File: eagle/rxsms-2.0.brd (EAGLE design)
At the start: 159 x 120.5 mm, 164 parts, among them Q1 opt, Q10 BSS123, Q11 BSS123, Q12 BSS123, Q2 BSS123, Q3 BSS123, Q4 BSS123, Q5 BSS123, Q6 BSS123, Q7 BSS123, Q8 BSS123, Q9 BSS123, T10_SODS SWITCH_LED, T1_LO SMS_IP67, T2_SOE SMS_IP67, T3_SOE SWITCH_LED, T4_PWR SMS_IP67, T5_ERRINH SMS_IP67, T6_PWR SWITCH_LED, T7_ERRINH SWITCH_LED, T8_LO SWITCH_LED, T9_SODS SMS_IP67, U1 MAX3232ESE, U2 XMEGA-A4UTQFP, U3 TSR_1-2450, U4 LM1117, U5 NC7WZ17P6X, U6 ADUM3160, U7 TPS73125, U8 NUP2202W1, X1 PN61729-S, X5 RLP2-200-500

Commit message: continued layout
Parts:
- moved C9 1.27 mm to (74.3, 21.6)
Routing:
- net RESERVED_IO_1: track 21.2 -> 18.3 mm
- net RESERVED_IO_0: track 25.2 -> 22.3 mm
- net GND: track 968.7 -> 966.0 mm, vias 17 -> 19
- net USB_VBUS: track 63.5 -> 62.8 mm
- net RESERVED_UART1_RX: track 14.1 -> 14.8 mm
- net N$16: track 41.2 -> 40.4 mm
- net +3V3: track 505.8 -> 506.5 mm

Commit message: fix: use correct lib name for TEN 3-2410N DCDC iso regulator
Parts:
- U$10: value TES3-4810WI -> TEN3-2410N; device TES3-4810WI:TES3-4810WI -> TEN3:TEN3-2410N
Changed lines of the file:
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@@
 <attribute name="OC_FARNELL" value="unknown" x="87.63" y="111.76" size="1.778" layer="27" display="off"/>
 </element>
-<element name="U$10" library="TES3-4810WI" package="TES3-4810WI" value="TES3-4810WI" x="58.42" y="48.26" rot="R180">
+<element name="U$10" library="TEN3" package="TEN3-2410N" value="TEN3-2410N" x="58.42" y="48.26" rot="R180">
 <attribute name="OC_RS" value="801-9330" x="58.42" y="48.26" size="1.778" layer="27" rot="R180" display="off"/>
 </element>

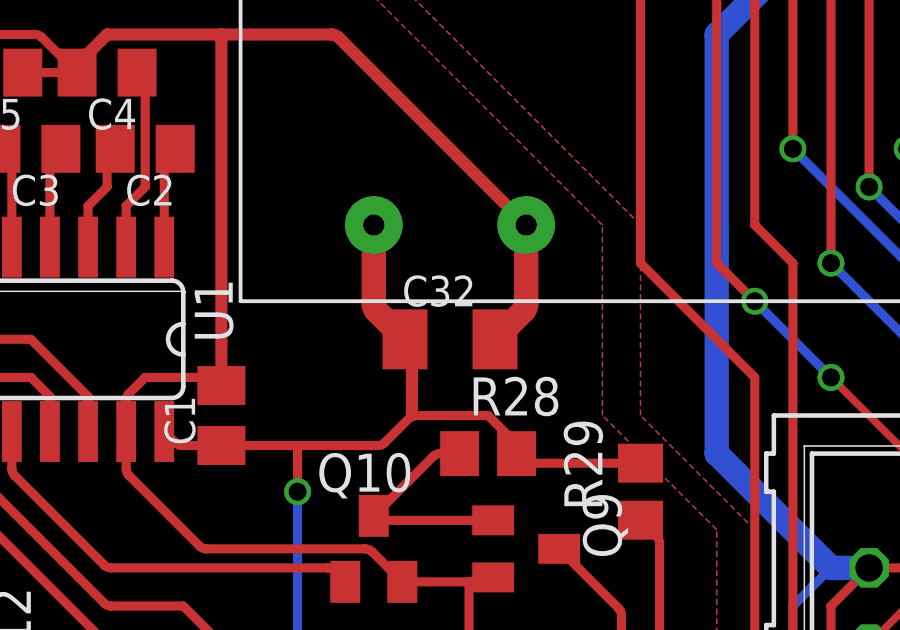
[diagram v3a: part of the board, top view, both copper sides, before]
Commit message: more OC added
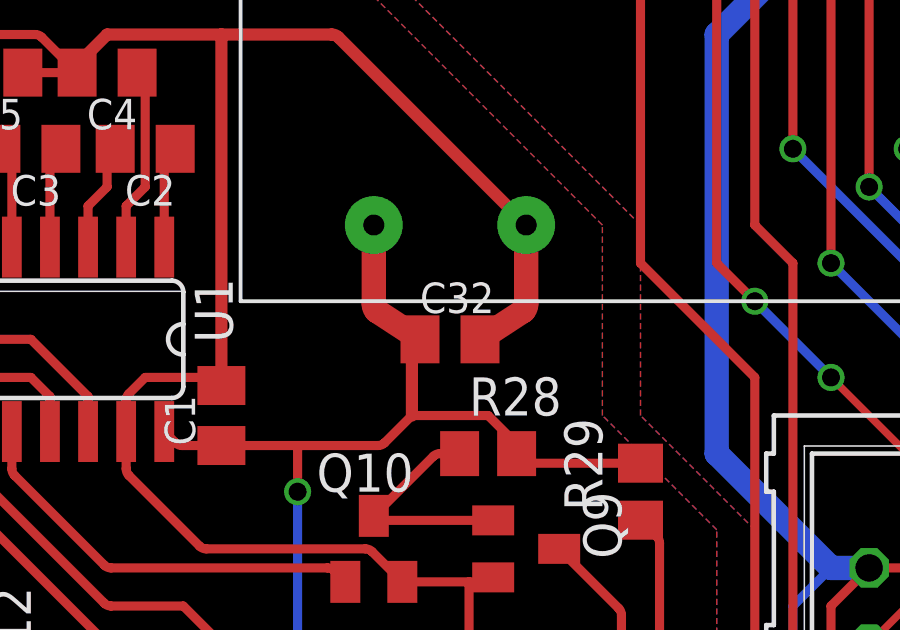
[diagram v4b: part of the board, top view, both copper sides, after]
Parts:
- C32: device rcl:C1206K -> rcl:C0805K
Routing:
- net VDD: track 65.6 -> 66.2 mm
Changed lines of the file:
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@@
 <attribute name="OC_FARNELL" value="1667008" x="83.82" y="29.21" size="1.778" layer="27" rot="R270" display="off"/>
 </element>
-<element name="U3" library="_traco_tsr-1" package="TSR-1" value="TSR_1-2450" x="78.74" y="91.44" rot="R270"/>
+<element name="U3" library="_traco_tsr-1" package="TSR-1" value="TSR_1-2450" x="78.74" y="91.44" rot="R270">
+<attribute name="OC_FARNELL" value="1696320" x="78.74" y="91.44" size="1.778" layer="27" rot="R270" display="off"/>
+</element>
 <element name="C12" library="rcl" package="C0805K" value="4u7/50V" x="62.23" y="85.09"/>
 <element name="C13" library="rcl" package="C0805K" value="4u7/50V" x="80.01" y="83.82"/>
@@
 <attribute name="OC_FARNELL" value="1887308" x="18.415" y="85.09" size="1.778" layer="27" rot="R270" display="off"/>
 </element>
-<element name="R4" library="rcl" package="R0805" value="22k" x="31.75" y="72.39" rot="R180"/>
-<element name="U$6" library="BTS6134" package="TO-252-5-1" value="BTS6143" x="26.67" y="104.14" rot="R270"/>
+<element name="R4" library="rcl" package="R0805" value="22k" x="31.75" y="72.39" rot="R180">
+<attribute name="OC_FARNELL" value="2303686" x="31.75" y="72.39" size="1.778" layer="27" rot="R180" display="off"/>
+</element>
+<element name="U$6" library="BTS6134" package="TO-252-5-1" value="BTS6143" x="26.67" y="104.14" rot="R270">
+<attribute name="OC_FARNELL" value="1440813" x="26.67" y="104.14" size="1.778" layer="27" rot="R270" display="off"/>
+</element>
 <element name="R5" library="rcl" package="R0805" value="10k" x="54.61" y="87.63" rot="R180">
 <attribute name="OC_FARNELL" value="1887308" x="54.61" y="87.63" size="1.778" layer="27" rot="R180" display="off"/>
@@
 <attribute name="OC_FARNELL" value="1887308" x="43.18" y="93.98" size="1.778" layer="27" rot="R270" display="off"/>
 </element>
-<element name="U6" library="adum3160" package="SO-16W" value="ADUM3160" x="113.03" y="10.16" rot="R90"/>
+<element name="U6" library="adum3160" package="SO-16W" value="ADUM3160" x="113.03" y="10.16" rot="R90">
+<attribute name="OC_FARNELL" value="1843660" x="113.03" y="10.16" size="1.778" layer="27" rot="R90" display="off"/>
+</element>
 <element name="C17" library="rcl" package="C0805K" value="&gt;100n/low ESR" x="123.19" y="8.255"/>
-<element name="R12" library="rcl" package="R0805" value="24/1%" x="124.46" y="11.43"/>
+<element name="R12" library="rcl" package="R0805" value="24/1%" x="124.46" y="11.43">
+<attribute name="OC_FARNELL" value="1894163" x="124.46" y="11.43" size="1.778" layer="27" display="off"/>
+</element>
 <element name="C18" library="rcl" package="C0805K" value="&gt;100n/low ESR" x="123.19" y="5.08"/>
-<element name="R13" library="rcl" package="R0805" value="24/1%" x="124.46" y="13.97"/>
+<element name="R13" library="rcl" package="R0805" value="24/1%" x="124.46" y="13.97">
+<attribute name="OC_FARNELL" value="1894163" x="124.46" y="13.97" size="1.778" layer="27" display="off"/>
+</element>
 <element name="C19" library="rcl" package="C0805K" value="&gt;100n/low ESR" x="104.14" y="7.62" rot="R270"/>
 <element name="C20" library="rcl" package="C0805K" value="&gt;100n/low ESR" x="101.6" y="7.62" rot="R270"/>
-<element name="R14" library="rcl" package="R0805" value="24/1%" x="99.6696" y="15.4813"/>
-<element name="R15" library="rcl" package="R0805" value="24/1%" x="97.4344" y="12.0015"/>
+<element name="R14" library="rcl" package="R0805" value="24/1%" x="99.6696" y="15.4813">
+<attribute name="OC_FARNELL" value="1894163" x="99.6696" y="15.4813" size="1.778" layer="27" display="off"/>
+</element>
+<element name="R15" library="rcl" package="R0805" value="24/1%" x="97.4344" y="12.0015">
+<attribute name="OC_FARNELL" value="1894163" x="97.4344" y="12.0015" size="1.778" layer="27" display="off"/>
+</element>
 <element name="U4" library="LM1117" package="TO252" value="LM1117" x="73.66" y="74.93" rot="R90"/>
 <element name="X1" library="con-berg" package="PN61729-S" value="PN61729-S" x="151.206384375" y="11" rot="R90">
@@
 <attribute name="MPN" value="" x="151.206384375" y="11" size="1.778" layer="27" rot="R90" display="off"/>
 <attribute name="MF" value="" x="151.206384375" y="11" size="1.778" layer="27" rot="R90" display="off"/>
-<attribute name="OC_FARNELL" value="unknown" x="151.206384375" y="11" size="1.778" layer="27" rot="R90" display="off"/>
-</element>
-<element name="U7" library="TPS731xx" package="SOT25" value="TPS73125" x="69.85" y="50.8" rot="R180"/>
+<attribute name="OC_FARNELL" value="1642035" x="151.206384375" y="11" size="1.778" layer="27" rot="R90" display="off"/>
+</element>
+<element name="U7" library="TPS731xx" package="SOT25" value="TPS73125" x="69.85" y="50.8" rot="R180">
+<attribute name="OC_FARNELL" value="2112625" x="69.85" y="50.8" size="1.778" layer="27" rot="R180" display="off"/>
+</element>
 <element name="U$7_BER" library="poti" package="VERT_POTI" value="" x="115" y="85" rot="R270"/>
 <element name="C21" library="rcl" package="C0805K" value="100n" x="68.58" y="46.99"/>
@@
 <element name="R20" library="rcl" package="R0805" value="1k" x="124.46" y="20.32" rot="R180"/>
 <element name="C29" library="rcl" package="C0805K" value="100n" x="124.46" y="17.78"/>
-<element name="C32" library="rcl" package="C1206K" value="10u/16V" x="38.1" y="44.45"/>
+<element name="C32" library="rcl" package="C0805K" value="10u/16V" x="38.1" y="44.45"/>
 <element name="C33" library="rcl" package="C0805K" value="100n" x="72.39" y="41.91" rot="R180"/>
 <element name="OK1" library="optocoupler" package="SOIC08" value="HCPL0600" x="36.83" y="25.4">
@@
 <element name="LED8" library="led" package="CHIPLED_1206" value="GREEN" x="69.85" y="83.82" rot="R90"/>
 <element name="U8" library="nup2202w1" package="SOT363_PHILIPS" value="NUP2202W1" x="131.445" y="8.89" rot="R180"/>
-<element name="C34" library="rcl" package="C0805K" value="4n7" x="143.51" y="16.51" rot="R180"/>
-<element name="R48" library="rcl" package="R0805" value="1M" x="143.51" y="13.97"/>
+<element name="C34" library="rcl" package="C0805K" value="4n7" x="143.51" y="16.51" rot="R180">
+<attribute name="OC_FARNELL" value="1759241" x="143.51" y="16.51" size="1.778" layer="27" rot="R180" display="off"/>
+</element>
+<element name="R48" library="rcl" package="R0805" value="1M" x="143.51" y="13.97">
+<attribute name="OC_FARNELL" value="2332111" x="143.51" y="13.97" size="1.778" layer="27" display="off"/>
+</element>
 <element name="LED7" library="led" package="CHIPLED_1206" value="BERNSTEIN" x="146.2" y="107.54" rot="R270">
 <attribute name="OC_FARNELL" value="2322083" x="146.2" y="107.54" size="1.778" layer="27" rot="R270" display="off"/>
@@
 <element name="U$7" library="holes" package="3,2" value="" x="137" y="14"/>
 <element name="U$8" library="holes" package="3,2" value="" x="137" y="106.5"/>
-<element name="D1" library="diode" package="SOT23" value="3V" x="33.655" y="69.215" rot="R90"/>
+<element name="D1" library="diode" package="SOT23" value="3V" x="33.655" y="69.215" rot="R90">
+<attribute name="OC_FARNELL" value="1081418" x="33.655" y="69.215" size="1.778" layer="27" rot="R90" display="off"/>
+</element>
 <element name="U5" library="NC7WZ17" package="SOT65P210X110-6N" value="NC7WZ17P6X" x="39.37" y="71.12">
 <attribute name="PACKAGE" value="SC-70-6" x="39.37" y="71.12" size="1.778" layer="27" display="off"/>
@@
 <wire x1="15.24" y1="58.9548875" x2="15.14700625" y2="59.17939375" width="0.3048" layer="1" curve="45"/>
 <wire x1="15.14700625" y1="59.17939375" x2="12.44" y2="61.8864" width="0.3048" layer="1"/>
-<wire x1="39.6" y1="44.45" x2="40.54700625" y2="45.39700625" width="0.8128" layer="1"/>
+<wire x1="39.1" y1="44.45" x2="40.54700625" y2="45.39700625" width="0.8128" layer="1"/>
 <wire x1="40.54700625" y1="45.39700625" x2="40.64" y2="45.6215125" width="0.8128" layer="1" curve="45"/>
 <wire x1="40.64" y1="45.6215125" x2="40.64" y2="48.26" width="0.8128" layer="1"/>
@@
 <via x="33.02" y="39.37" extent="1-16" drill="0.6"/>
 <wire x1="33.02" y1="39.37" x2="33.02" y2="40.91" width="0.3048" layer="1"/>
-<wire x1="36.6" y1="44.45" x2="35.65299375" y2="45.39700625" width="0.8128" layer="1"/>
+<wire x1="37.1" y1="44.45" x2="35.65299375" y2="45.39700625" width="0.8128" layer="1"/>
 <wire x1="35.65299375" y1="45.39700625" x2="35.56" y2="45.6215125" width="0.8128" layer="1" curve="-45"/>
 <wire x1="35.56" y1="45.6215125" x2="35.56" y2="48.26" width="0.8128" layer="1"/>
-<wire x1="36.6" y1="44.45" x2="36.73700625" y2="44.31299375" width="0.4064" layer="1"/>
+<wire x1="37.1" y1="44.45" x2="36.73700625" y2="44.31299375" width="0.4064" layer="1"/>
 <wire x1="36.73700625" y1="44.31299375" x2="36.83" y2="44.0884875" width="0.4064" layer="1" curve="-45"/>
 <wire x1="36.83" y1="44.0884875" x2="36.83" y2="41.91" width="0.4064" layer="1"/>

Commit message: added even more OC
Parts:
- C17, C18, C19, C20: value >100n/low ESR -> 1u
- R29, R32: value 267 -> 270
- R43, R44: value 220 -> 68
- R49: value 220 -> 150
- U$7_BER, U$8_DROPR, U$9_DROPDUR: value (none) -> 50k
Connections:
- net GND: now also U5.3
